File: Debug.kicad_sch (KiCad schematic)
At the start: 30 parts, among them J501 USB1, U501 FT2232HQ, U502 93LCxxBxxOT, Y501 12M

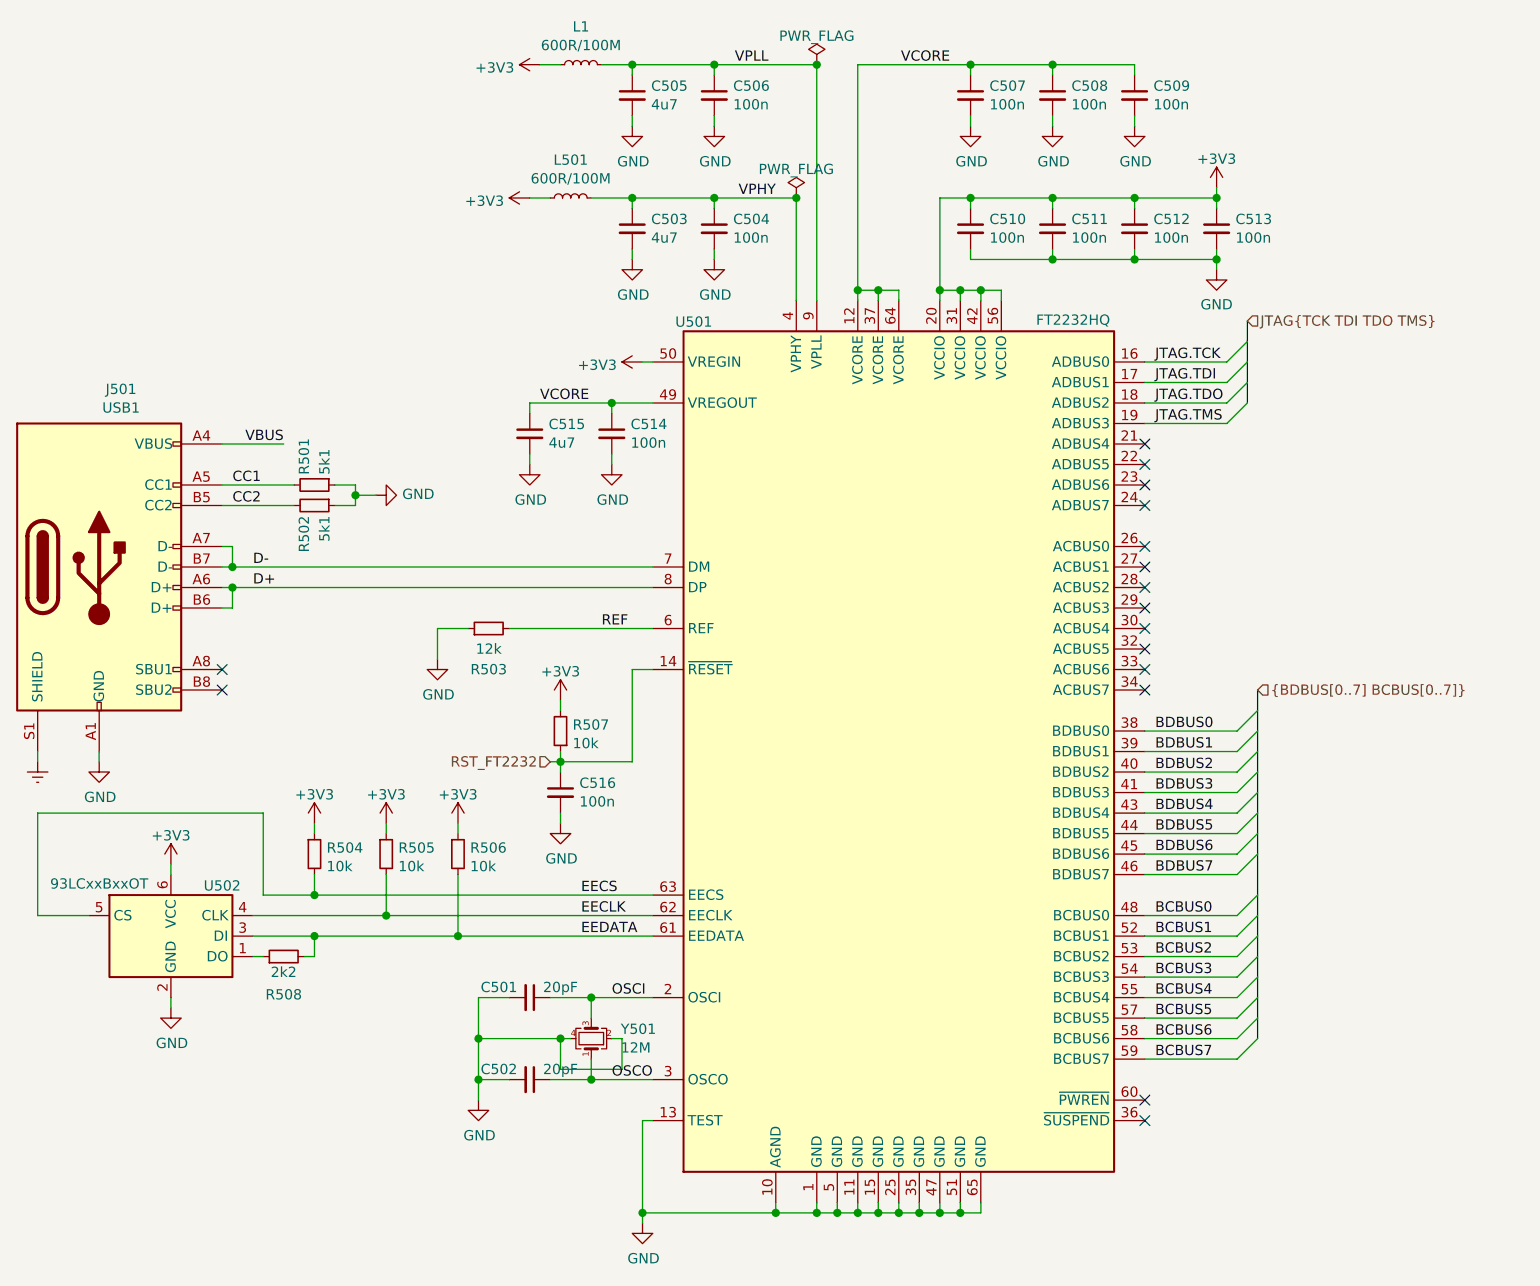
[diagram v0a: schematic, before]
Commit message: Update to KiCad 6
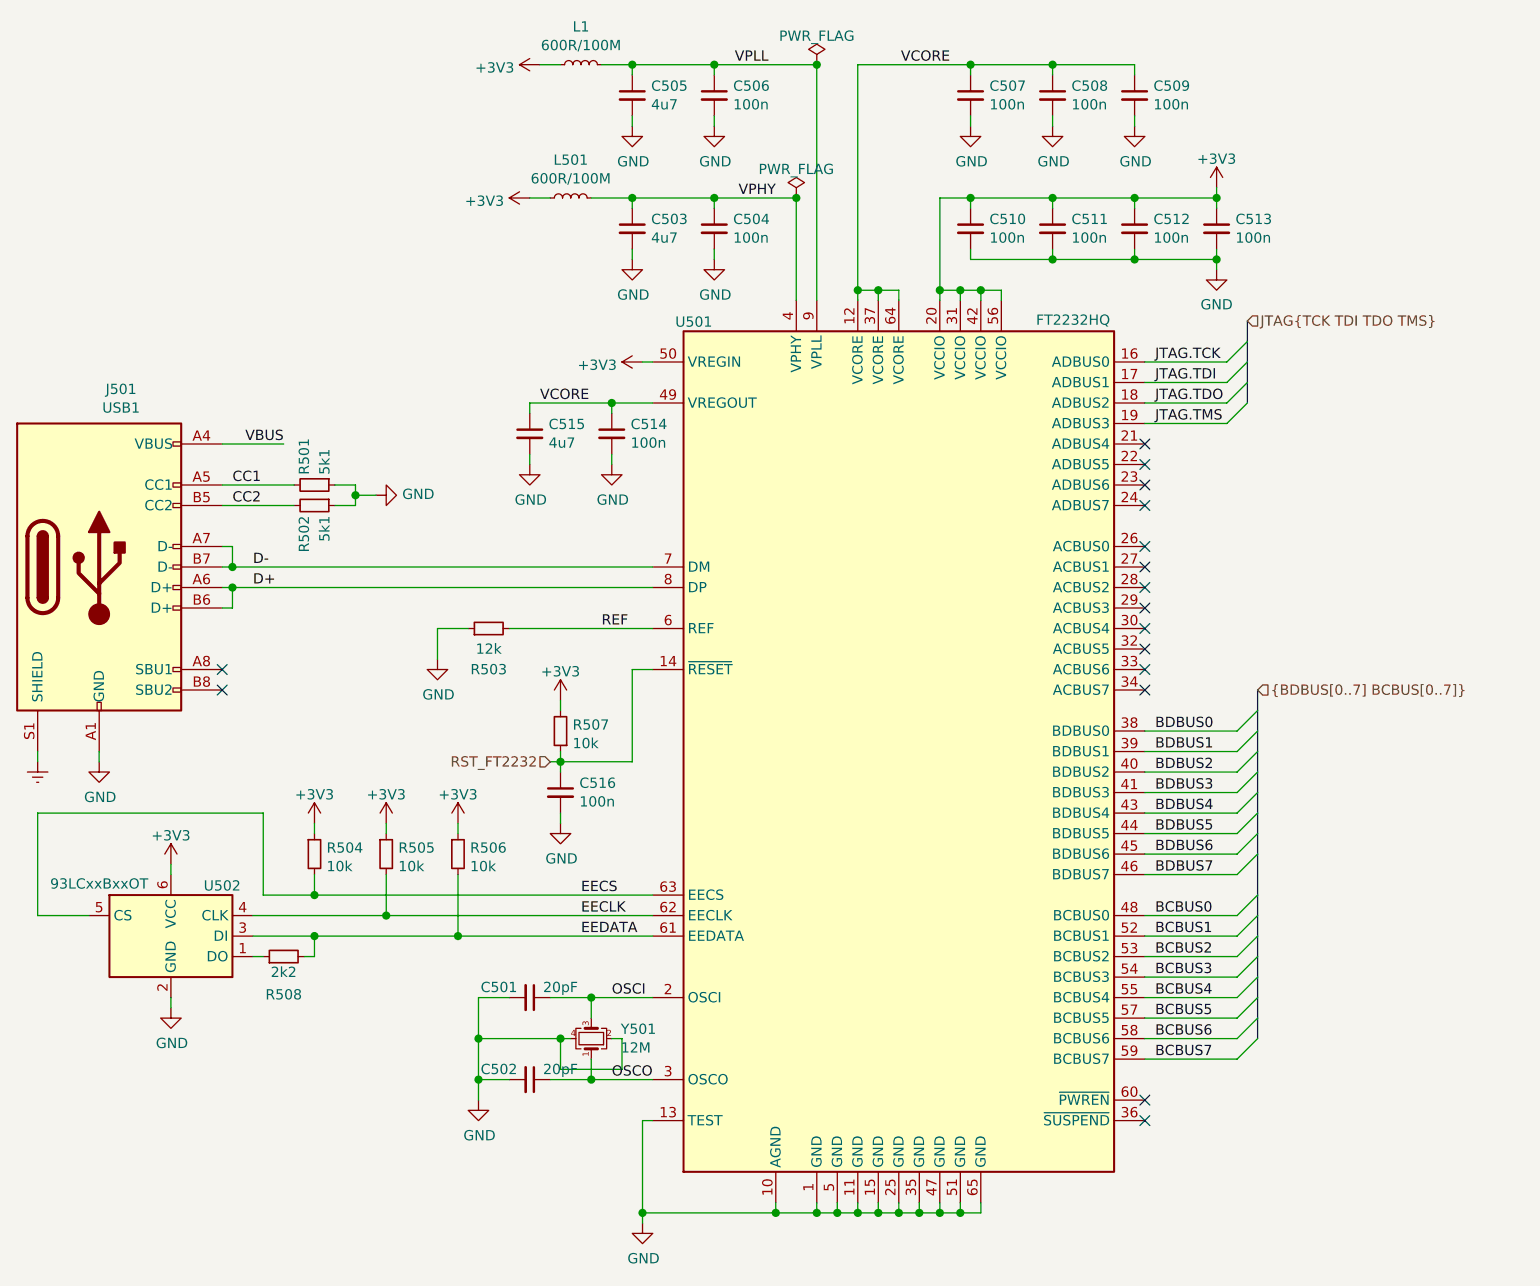
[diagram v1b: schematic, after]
